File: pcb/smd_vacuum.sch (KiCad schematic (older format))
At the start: 25 parts, among them J1 PWR, M1 Motor_DC, Q1 Q_PMOS_GDS, Q2 Q_NMOS_GDS, Q3 Q_NMOS_GDS, SW1 SW_SPST, U1 NE555P, U2 EL817

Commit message: board layout
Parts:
- added H1, H2, H3, H4: MountingHole, MountingHole:MountingHole_3.2mm_M3, symbol Mechanical:MountingHole
- D1, D3, D4: footprint (none) -> Connector_JST:JST_PH_B2B-PH-K_1x02_P2.00mm_Vertical
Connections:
- net +12V: now also L1.2; no longer L1.1
- net at D6.2 (A), Q3.2 (D): now also L1.1; no longer L1.2
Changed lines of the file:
@@
 F 0 "D4" H 7550 3550 50  0000 C CNN
 F 1 "LED" H 7550 3350 50  0000 C CNN
-F 2 "" H 7550 3450 50  0001 C CNN
+F 2 "Connector_JST:JST_PH_B2B-PH-K_1x02_P2.00mm_Vertical" H 7550 3450 50  0001 C CNN
 F 3 "~" H 7550 3450 50  0001 C CNN
 	1    7550 3450
@@
 F 3 "" H 8300 3450 50  0001 C CNN
 	1    8300 3450
-	1    0    0    -1
-$EndComp
-$Comp
-L Motor:Motor_DC M1
-U 1 1 60859C35
-P 8600 2550
-F 0 "M1" H 8700 2650 50  0000 L CNN
-F 1 "Motor_DC" H 8700 2350 50  0000 L TNN
-F 2 "pl_TerminalBlock:WJ127-5.0-2P" H 8600 2460 50  0001 C CNN
-F 3 "~" H 8600 2460 50  0001 C CNN
-	1    8600 2550
 	1    0    0    -1
 $EndComp
@@
 F 0 "D3" H 5400 5550 50  0000 C CNN
 F 1 "LED" H 5400 5350 50  0000 C CNN
-F 2 "" H 5400 5450 50  0001 C CNN
+F 2 "Connector_JST:JST_PH_B2B-PH-K_1x02_P2.00mm_Vertical" H 5400 5450 50  0001 C CNN
 F 3 "~" H 5400 5450 50  0001 C CNN
 	1    5400 5450
@@
 F 3 "~" H 8650 4900 50  0001 C CNN
 	1    8650 4900
-	1    0    0    -1
+	1    0    0    1
 $EndComp
 Wire Wire Line
@@
 F 0 "D1" H 4000 2350 50  0000 C CNN
 F 1 "LED" H 4000 2150 50  0000 C CNN
-F 2 "" H 4000 2250 50  0001 C CNN
+F 2 "Connector_JST:JST_PH_B2B-PH-K_1x02_P2.00mm_Vertical" H 4000 2250 50  0001 C CNN
 F 3 "~" H 4000 2250 50  0001 C CNN
 	1    4000 2250
@@
 Wire Wire Line
 	1500 7000 1500 7200
+$Comp
+L Motor:Motor_DC M1
+U 1 1 60859C35
+P 8600 2550
+F 0 "M1" H 8700 2650 50  0000 L CNN
+F 1 "Motor_DC" H 8700 2350 50  0000 L TNN
+F 2 "pl_TerminalBlock:WJ127-5.0-2P" H 8600 2460 50  0001 C CNN
+F 3 "~" H 8600 2460 50  0001 C CNN
+	1    8600 2550
+	1    0    0    -1
+$EndComp
+$Comp
+L Mechanical:MountingHole H1
+U 1 1 60B08B99
+P 1500 5000
+F 0 "H1" H 1500 5200 50  0000 C CNN
+F 1 "MountingHole" H 1500 5125 50  0000 C CNN
+F 2 "MountingHole:MountingHole_3.2mm_M3" H 1500 5000 50  0001 C CNN
+F 3 "~" H 1500 5000 50  0001 C CNN
+	1    1500 5000
+	1    0    0    -1
+$EndComp
+$Comp
+L Mechanical:MountingHole H3
+U 1 1 60B0987F
+P 2000 5000
+F 0 "H3" H 2000 5200 50  0000 C CNN
+F 1 "MountingHole" H 2000 5125 50  0000 C CNN
+F 2 "MountingHole:MountingHole_3.2mm_M3" H 2000 5000 50  0001 C CNN
+F 3 "~" H 2000 5000 50  0001 C CNN
+	1    2000 5000
+	1    0    0    -1
+$EndComp
+$Comp
+L Mechanical:MountingHole H4
+U 1 1 60B099EF
+P 2000 5500
+F 0 "H4" H 2000 5700 50  0000 C CNN
+F 1 "MountingHole" H 2000 5625 50  0000 C CNN
+F 2 "MountingHole:MountingHole_3.2mm_M3" H 2000 5500 50  0001 C CNN
+F 3 "~" H 2000 5500 50  0001 C CNN
+	1    2000 5500
+	1    0    0    -1
+$EndComp
+$Comp
+L Mechanical:MountingHole H2
+U 1 1 60B09C6F
+P 1500 5500
+F 0 "H2" H 1500 5700 50  0000 C CNN
+F 1 "MountingHole" H 1500 5625 50  0000 C CNN
+F 2 "MountingHole:MountingHole_3.2mm_M3" H 1500 5500 50  0001 C CNN
+F 3 "~" H 1500 5500 50  0001 C CNN
+	1    1500 5500
+	1    0    0    -1
+$EndComp
 $EndSCHEMATC

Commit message: add polarity protection pmos part number
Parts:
- Q1: value Q_PMOS_GDS -> IRF5305
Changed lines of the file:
@@
 P 3600 2100
 F 0 "Q1" V 3550 2200 50  0000 L CNN
-F 1 "Q_PMOS_GDS" V 3850 2100 50  0000 C CNN
+F 1 "IRF5305" V 3850 2100 50  0000 C CNN
 F 2 "Package_TO_SOT_THT:TO-220-3_Vertical" H 3800 2200 50  0001 C CNN
 F 3 "~" H 3600 2100 50  0001 C CNN

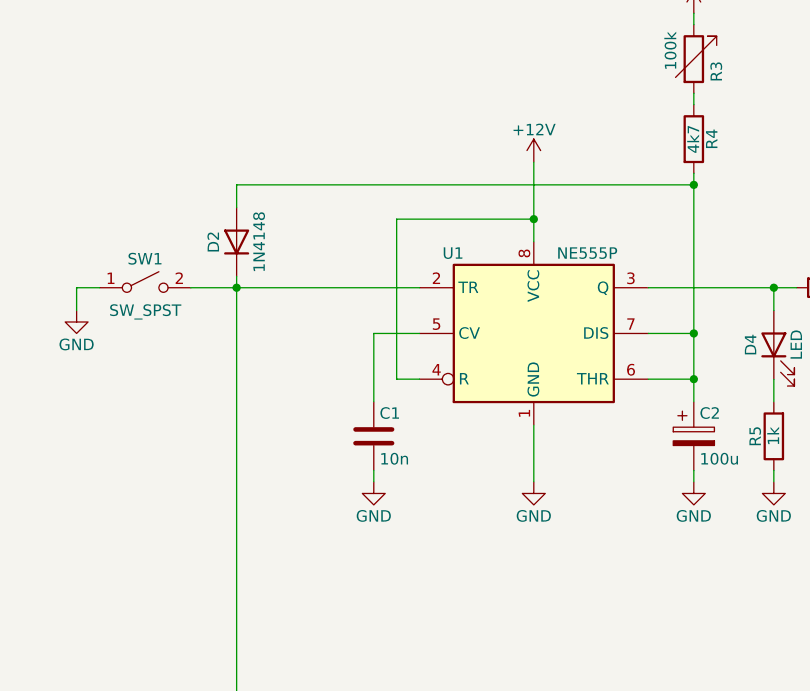
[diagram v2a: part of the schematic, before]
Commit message: add rc to 555 reset for power on reset
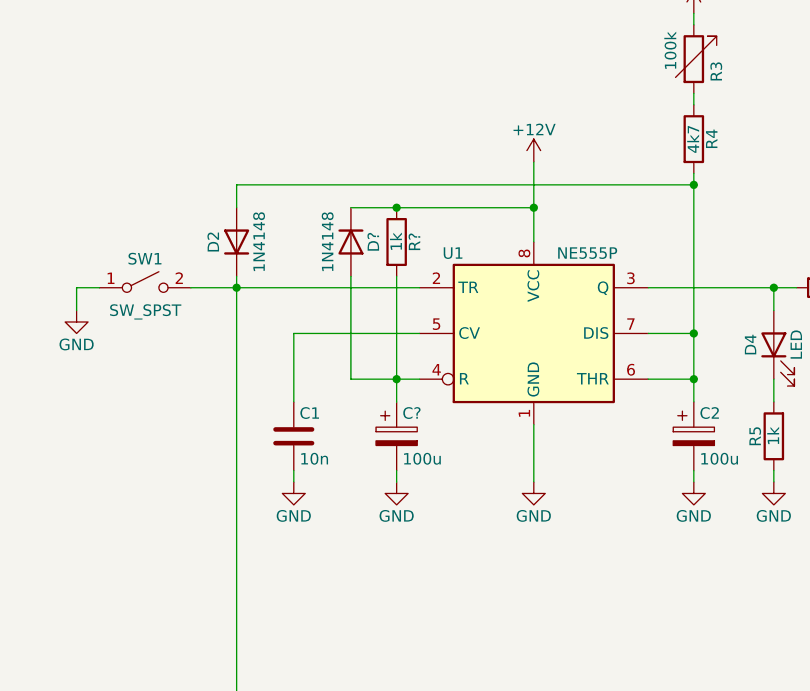
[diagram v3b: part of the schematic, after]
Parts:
- added C?: 100u, symbol Device:CP
- added D?: 1N4148, Diode_THT:D_DO-35_SOD27_P7.62mm_Horizontal, symbol Diode:1N4148
- added R?: 1k, symbol Device:R
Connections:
- net +12V: now also D?.1 (K), R?.1; no longer U1.4 (R)
- net GND: now also C?.2
- new net: C?.1, D?.2 (A), R?.2, U1.4 (R)
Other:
- moved on the sheet: C1
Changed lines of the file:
@@
 L Device:C C1
 U 1 1 60861E64
-P 5800 3850
-F 0 "C1" H 5825 3950 50  0000 L CNN
-F 1 "10n" H 5825 3750 50  0000 L CNN
-F 2 "Capacitor_THT:C_Rect_L7.0mm_W3.5mm_P5.00mm" H 5838 3700 50  0001 C CNN
-F 3 "~" H 5800 3850 50  0001 C CNN
-	1    5800 3850
+P 5450 3850
+F 0 "C1" H 5475 3950 50  0000 L CNN
+F 1 "10n" H 5475 3750 50  0000 L CNN
+F 2 "Capacitor_THT:C_Rect_L7.0mm_W3.5mm_P5.00mm" H 5488 3700 50  0001 C CNN
+F 3 "~" H 5450 3850 50  0001 C CNN
+	1    5450 3850
 	1    0    0    -1
 $EndComp
@@
 Wire Wire Line
 	6500 3800 6500 4050
-Wire Wire Line
-	6500 3000 6500 2900
 $Comp
 L power:+12V #PWR011
@@
 	6000 3600 5900 3600
 Wire Wire Line
-	5900 3600 5900 2900
-Wire Wire Line
-	5900 2900 6500 2900
-Connection ~ 6500 2900
-Wire Wire Line
-	6500 2900 6500 2650
-Wire Wire Line
-	5800 3700 5800 3400
-Wire Wire Line
-	5800 3400 6000 3400
+	5450 3700 5450 3400
+Wire Wire Line
+	5450 3400 6000 3400
 $Comp
 L power:GND #PWR06
 U 1 1 608D8DFF
-P 5800 4050
-F 0 "#PWR06" H 5800 3800 50  0001 C CNN
-F 1 "GND" H 5800 3900 50  0000 C CNN
-F 2 "" H 5800 4050 50  0001 C CNN
-F 3 "" H 5800 4050 50  0001 C CNN
-	1    5800 4050
-	1    0    0    -1
-$EndComp
-Wire Wire Line
-	5800 4050 5800 4000
+P 5450 4050
+F 0 "#PWR06" H 5450 3800 50  0001 C CNN
+F 1 "GND" H 5450 3900 50  0000 C CNN
+F 2 "" H 5450 4050 50  0001 C CNN
+F 3 "" H 5450 4050 50  0001 C CNN
+	1    5450 4050
+	1    0    0    -1
+$EndComp
+Wire Wire Line
+	5450 4050 5450 4000
 Wire Wire Line
 	5200 2850 5200 2750
@@
 	1    0    0    -1
 $EndComp
+$Comp
+L Device:CP C?
+U 1 1 60890CB0
+P 5900 3850
+F 0 "C?" H 5925 3950 50  0000 L CNN
+F 1 "100u" H 5925 3750 50  0000 L CNN
+F 2 "" H 5938 3700 50  0001 C CNN
+F 3 "~" H 5900 3850 50  0001 C CNN
+	1    5900 3850
+	1    0    0    -1
+$EndComp
+$Comp
+L power:GND #PWR?
+U 1 1 60892189
+P 5900 4050
+F 0 "#PWR?" H 5900 3800 50  0001 C CNN
+F 1 "GND" H 5900 3900 50  0000 C CNN
+F 2 "" H 5900 4050 50  0001 C CNN
+F 3 "" H 5900 4050 50  0001 C CNN
+	1    5900 4050
+	1    0    0    -1
+$EndComp
+Wire Wire Line
+	5900 4050 5900 4000
+Wire Wire Line
+	5900 3700 5900 3600
+$Comp
+L Device:R R?
+U 1 1 608977FD
+P 5900 3000
+F 0 "R?" V 5980 3000 50  0000 C CNN
+F 1 "1k" V 5900 3000 50  0000 C CNN
+F 2 "" V 5830 3000 50  0001 C CNN
+F 3 "~" H 5900 3000 50  0001 C CNN
+	1    5900 3000
+	1    0    0    -1
+$EndComp
+Wire Wire Line
+	6500 2650 6500 2850
+Wire Wire Line
+	5900 2850 6500 2850
+Connection ~ 6500 2850
+Wire Wire Line
+	6500 2850 6500 3000
+Wire Wire Line
+	5900 3150 5900 3600
+Connection ~ 5900 3600
+$Comp
+L Diode:1N4148 D?
+U 1 1 6089BB67
+P 5700 3000
+F 0 "D?" H 5700 3100 50  0000 C CNN
+F 1 "1N4148" H 5700 2900 50  0000 C CNN
+F 2 "Diode_THT:D_DO-35_SOD27_P7.62mm_Horizontal" H 5700 2825 50  0001 C CNN
+F 3 "https://assets.nexperia.com/documents/data-sheet/1N4148_1N4448.pdf" H 5700 3000 50  0001 C CNN
+	1    5700 3000
+	0    1    1    0
+$EndComp
+Wire Wire Line
+	5700 2850 5900 2850
+Connection ~ 5900 2850
+Wire Wire Line
+	5700 3150 5700 3600
+Wire Wire Line
+	5700 3600 5900 3600
 $EndSCHEMATC

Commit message: layout pcb with reset circuitry
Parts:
- C3: renamed from C?; footprint (none) -> Capacitor_THT:CP_Radial_D8.0mm_P3.50mm
- R9: renamed from R?; footprint (none) -> Resistor_THT:R_Axial_DIN0207_L6.3mm_D2.5mm_P10.16mm_Horizontal
- gave numbers to parts that had none: 1
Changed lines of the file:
@@
 $EndComp
 $Comp
-L Device:CP C?
+L Device:CP C3
 U 1 1 60890CB0
 P 5900 3850
-F 0 "C?" H 5925 3950 50  0000 L CNN
+F 0 "C3" H 5925 3950 50  0000 L CNN
 F 1 "100u" H 5925 3750 50  0000 L CNN
-F 2 "" H 5938 3700 50  0001 C CNN
+F 2 "Capacitor_THT:CP_Radial_D8.0mm_P3.50mm" H 5938 3700 50  0001 C CNN
 F 3 "~" H 5900 3850 50  0001 C CNN
 	1    5900 3850
@@
 $EndComp
 $Comp
-L power:GND #PWR?
+L power:GND #PWR019
 U 1 1 60892189
 P 5900 4050
-F 0 "#PWR?" H 5900 3800 50  0001 C CNN
+F 0 "#PWR019" H 5900 3800 50  0001 C CNN
 F 1 "GND" H 5900 3900 50  0000 C CNN
 F 2 "" H 5900 4050 50  0001 C CNN
@@
 	5900 3700 5900 3600
 $Comp
-L Device:R R?
+L Device:R R9
 U 1 1 608977FD
 P 5900 3000
-F 0 "R?" V 5980 3000 50  0000 C CNN
+F 0 "R9" V 5980 3000 50  0000 C CNN
 F 1 "1k" V 5900 3000 50  0000 C CNN
-F 2 "" V 5830 3000 50  0001 C CNN
+F 2 "Resistor_THT:R_Axial_DIN0207_L6.3mm_D2.5mm_P10.16mm_Horizontal" V 5830 3000 50  0001 C CNN
 F 3 "~" H 5900 3000 50  0001 C CNN
 	1    5900 3000
@@
 Connection ~ 5900 3600
 $Comp
-L Diode:1N4148 D?
+L Diode:1N4148 D7
 U 1 1 6089BB67
 P 5700 3000
-F 0 "D?" H 5700 3100 50  0000 C CNN
+F 0 "D7" H 5700 3100 50  0000 C CNN
 F 1 "1N4148" H 5700 2900 50  0000 C CNN
 F 2 "Diode_THT:D_DO-35_SOD27_P7.62mm_Horizontal" H 5700 2825 50  0001 C CNN
